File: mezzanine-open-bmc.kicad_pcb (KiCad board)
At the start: 2 copper layers, 85 x 54.1 mm, 48 parts, among them P1 CONN_02X20, P2 CONN_02X20, SW1 PWR, SW2 RST, U1 FT230XS, U2 PMIC-CJT1117-3.3(SOT223), U4 PCA9306

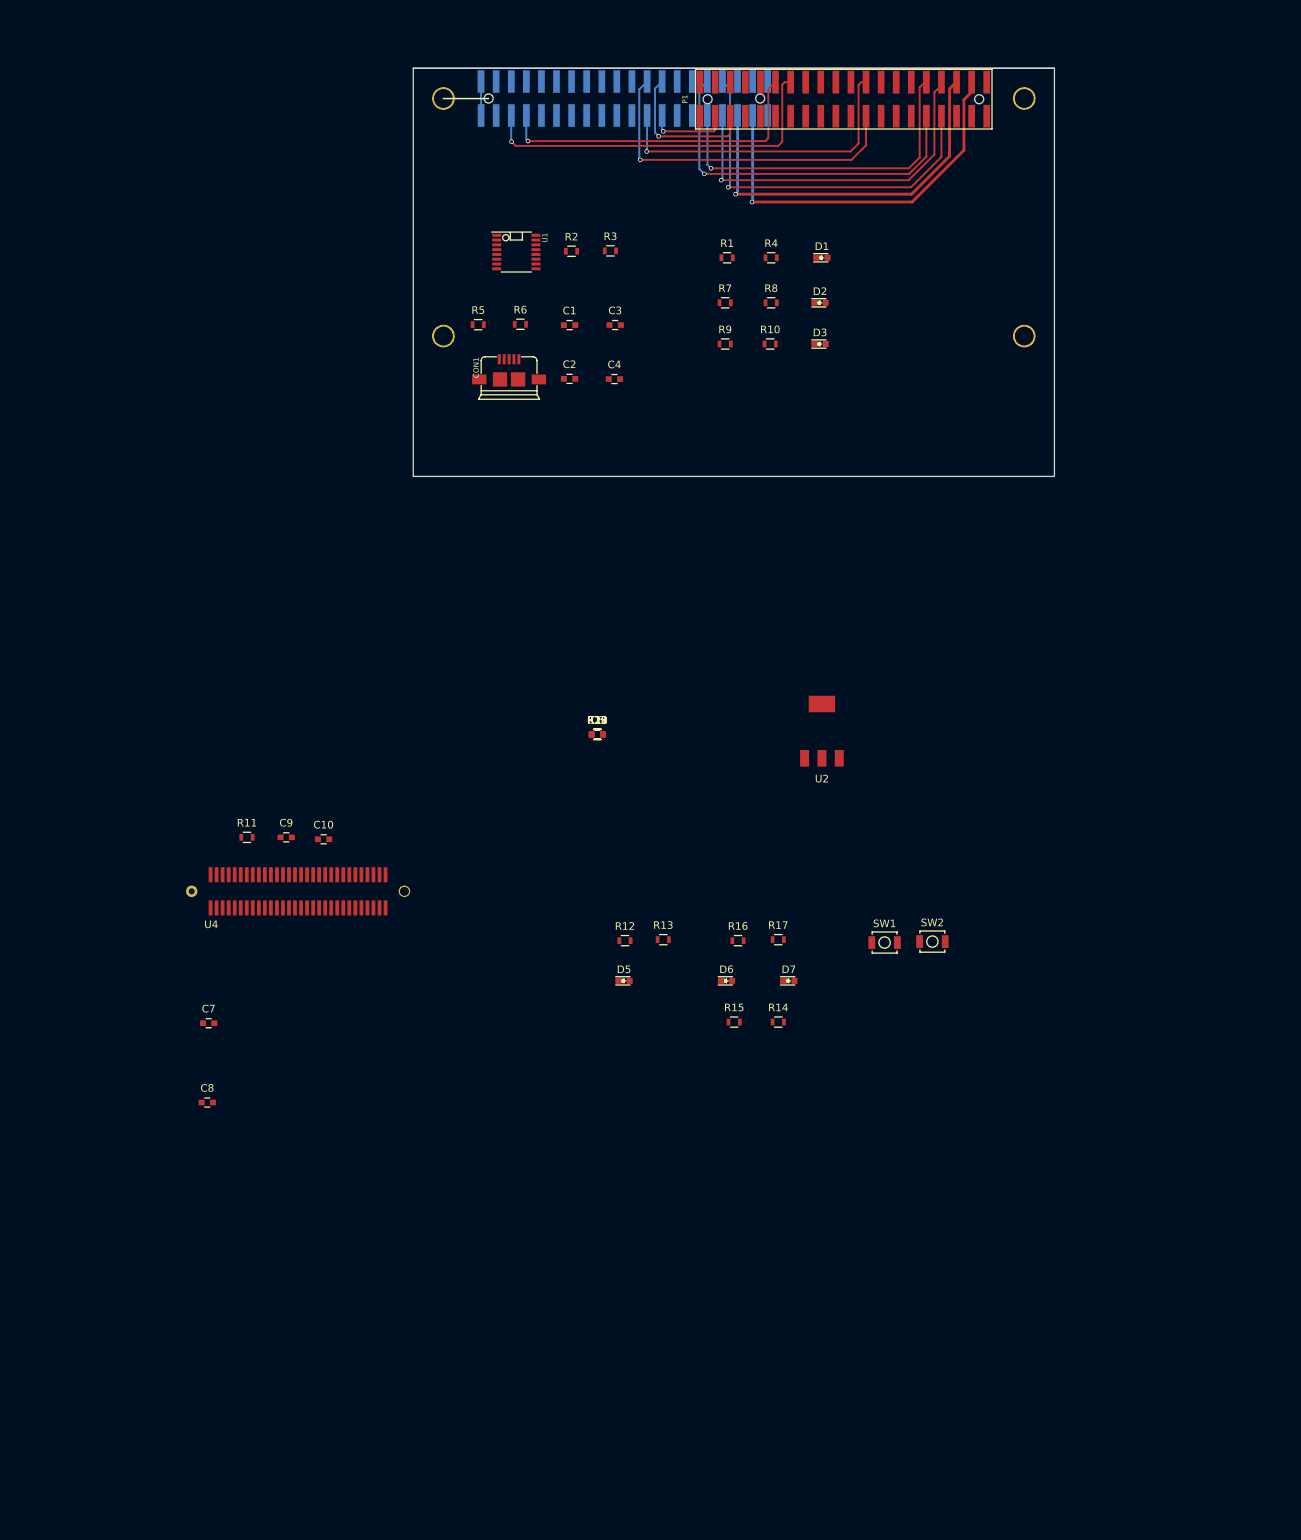
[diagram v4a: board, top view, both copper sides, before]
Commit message: Alternative Traces for Header Pins
Since most components will be sitting on the top side of the
device, traces for the header pins have been drawn on the bottom side
as much as possible. This should mean it will be easier to connect the
rest of the components.
A new branch has been made to preserve the former trace layout if this
version is no good.

Signed-off-by: Sophie Haynes <sophie.haynes@linaro.org>
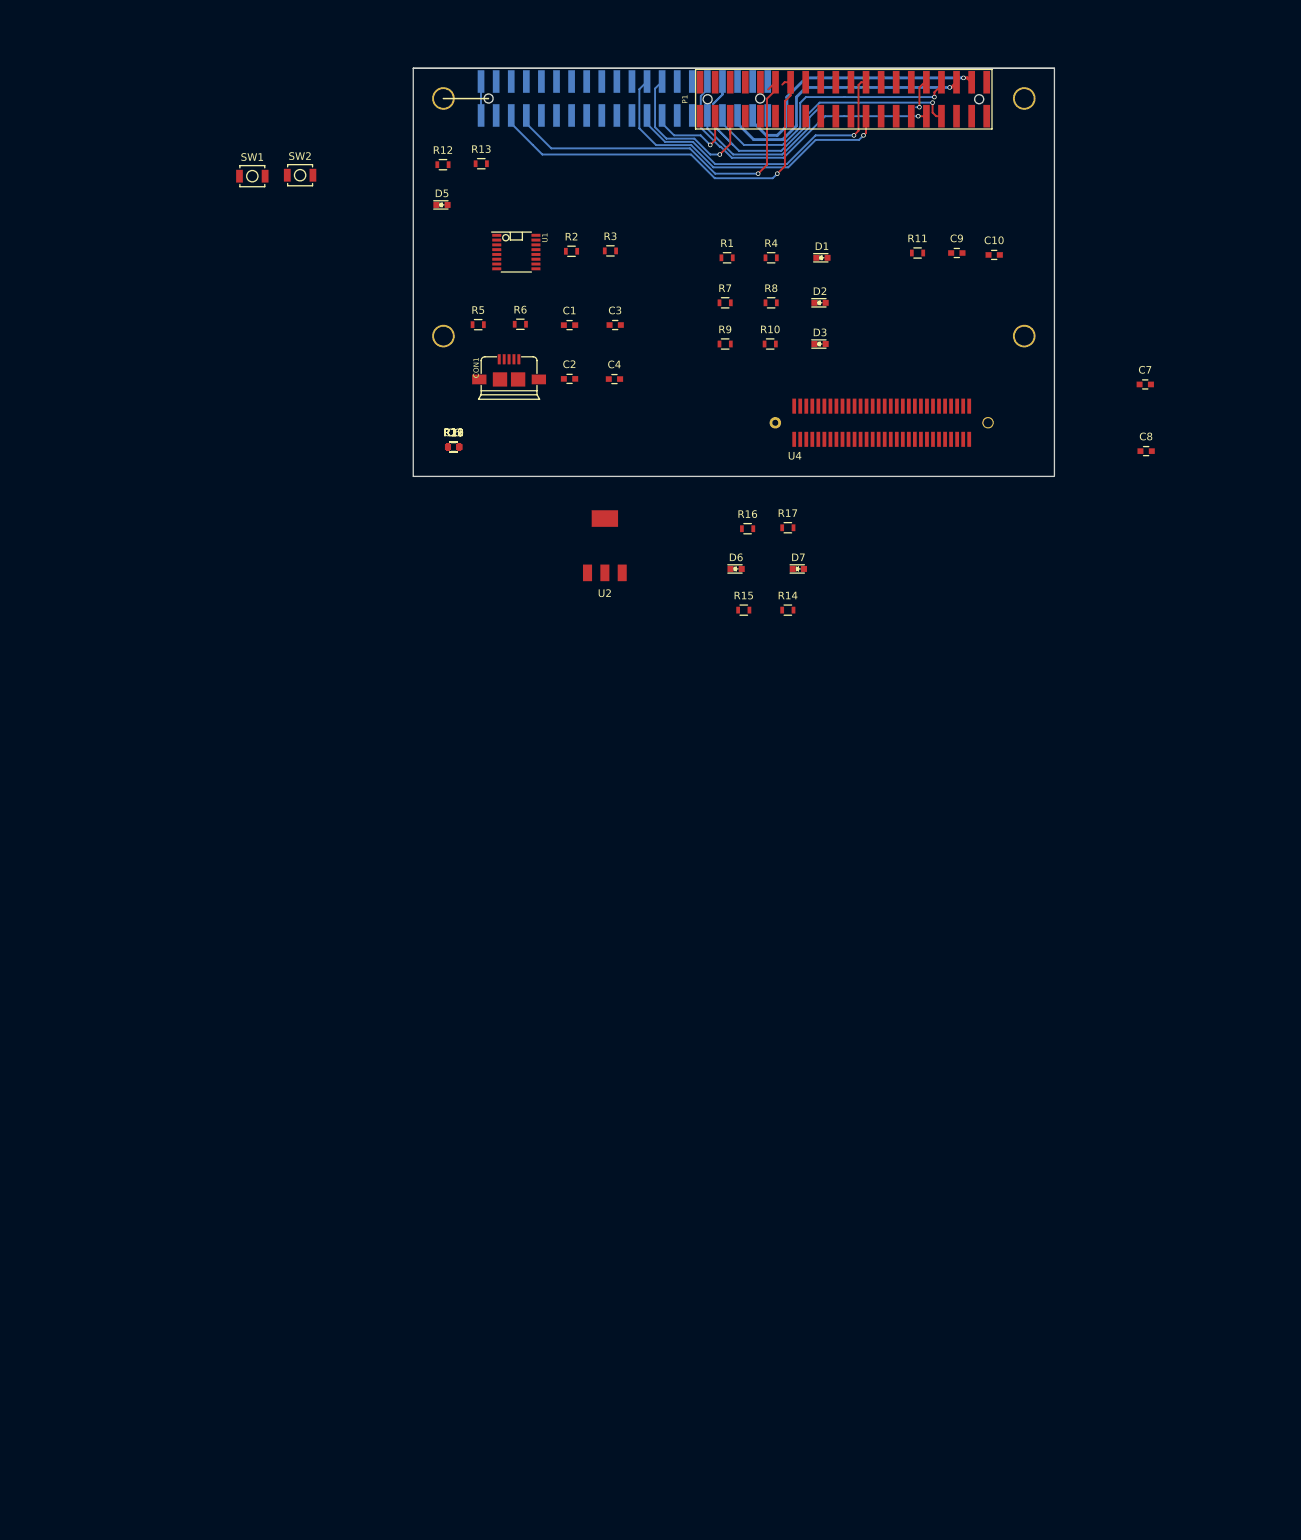
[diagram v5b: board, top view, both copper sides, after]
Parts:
- moved C8 151.5 mm to (197.2, 150.7)
- moved C7 150.3 mm to (197.0, 141.9)
- moved SW1 131.7 mm to (78.7, 114.3)
- moved SW2 131.7 mm to (85.0, 114.2)
- moved C10 117.9 mm to (177.0, 124.7)
- moved C9 117.9 mm to (172.1, 124.5)
- moved R11 117.9 mm to (166.9, 124.5)
- moved R13 105.7 mm to (109.0, 112.6)
- moved D5 105.7 mm to (103.8, 118.1)
- moved R12 105.7 mm to (103.9, 112.8)
- moved U4 99.2 mm to (150.5, 144.8)
- moved R14 54.6 mm to (149.7, 171.8)
- moved R15 54.6 mm to (143.8, 171.8)
- moved R17 54.6 mm to (149.7, 160.9)
- moved D6 54.6 mm to (142.8, 166.4)
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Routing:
- net GPIO_I: track 45.9 -> 25.7 mm
- net +1V8: track 51.2 -> 36.4 mm
- net +5V: track 51.9 -> 37.5 mm
- net GPIO_K: track 48.3 -> 37.2 mm
- net GPIO_J: track 48.7 -> 40.3 mm
- net UART0_RX_BMC: track 43.3 -> 49.0 mm
- net UART0_TX_BMC: track 48.7 -> 53.7 mm
- net GPIO_D_BMC: track 19.8 -> 24.5 mm
- net GPIO_L: track 49.9 -> 54.2 mm
- net GPIO_C_BMC: track 11.0 -> 14.5 mm
- net GPIO_B: track 45.4 -> 42.9 mm
- net GPIO_A: track 42.2 -> 40.4 mm

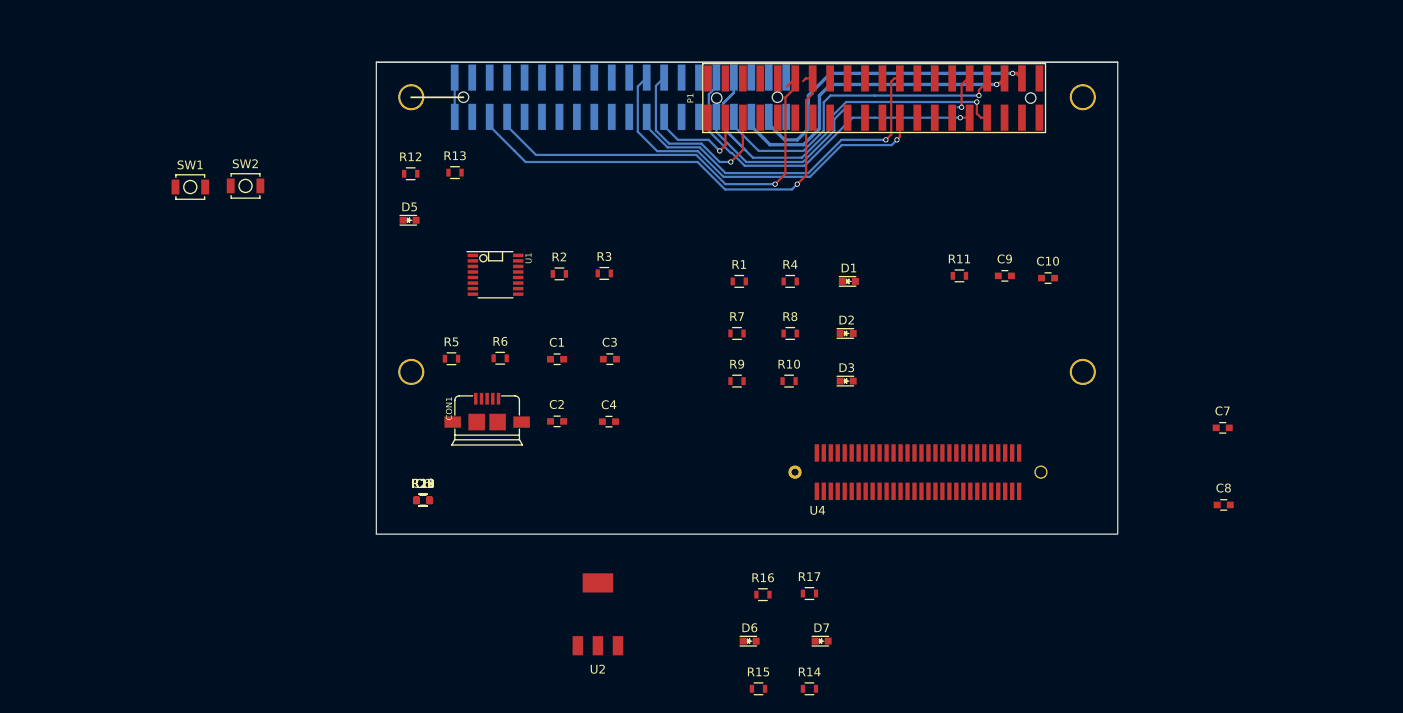
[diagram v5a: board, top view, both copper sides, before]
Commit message: Create Correct Footprint for PCA9306, Assign Footprint, Connect U4
The PCA footprint was incorrect. This has been fixed; there are two
different models so both types have been added. It has been assigned
accordingly in the schematic.

U4(level shifter 1.8-3.3v) has been connected up.

Signed-off-by: Sophie Haynes <sophie.haynes@linaro.org>
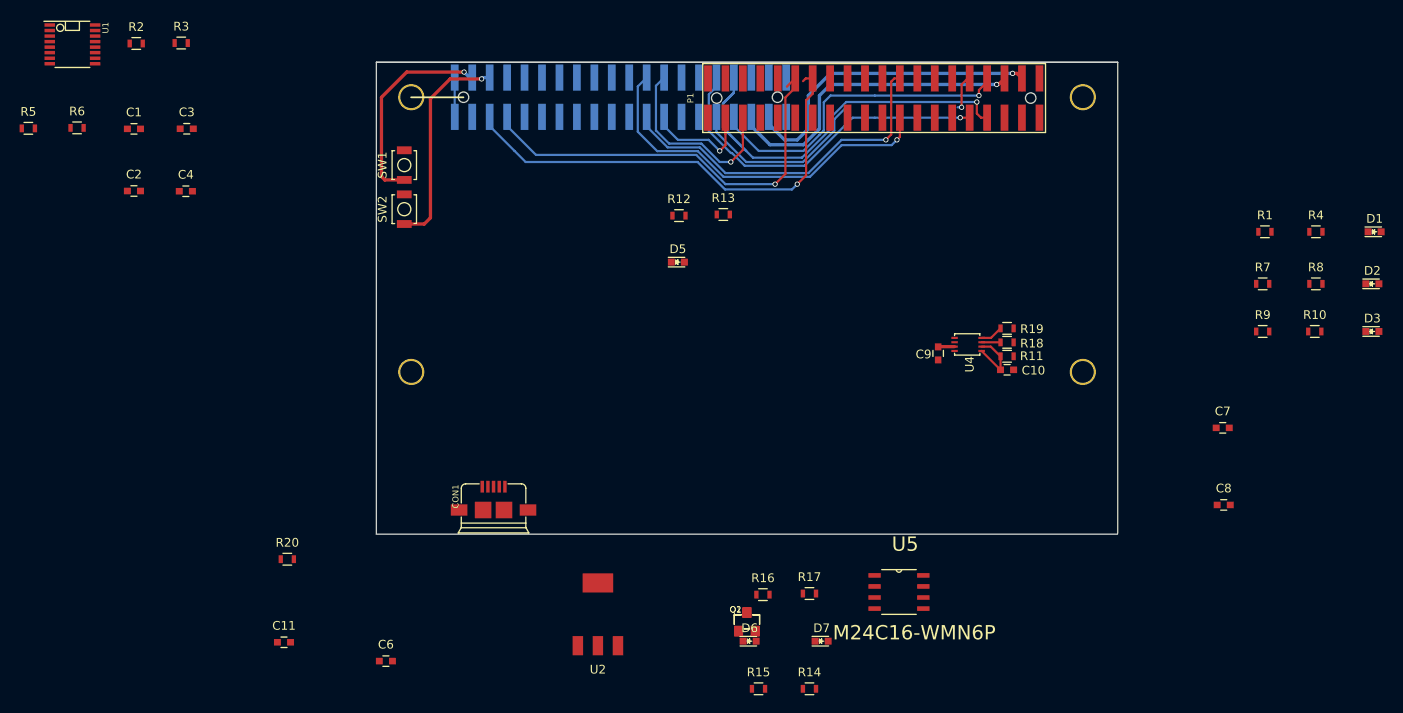
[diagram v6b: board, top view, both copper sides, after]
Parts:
- added Q1, Q2: S8050, 96boards:SOT-23_Seeed, F.Cu at (142.5, 164.2)
- added U5: M24C16-WMN6P, 96boards:SOIC127P600X175-8N, F.Cu at (159.9, 160.7)
- moved R19 69.8 mm to (172.3, 130.5), turned to 180 degrees
- moved R18 69.4 mm to (172.3, 132.1), turned to 180 degrees
- moved D1 60.5 mm to (214.5, 119.4)
- moved R1 60.5 mm to (201.9, 119.4)
- moved R10 60.5 mm to (207.6, 130.9)
- moved R7 60.5 mm to (201.6, 125.4)
- moved R9 60.5 mm to (201.6, 130.9)
- moved D2 60.5 mm to (214.2, 125.4)
- moved D3 60.5 mm to (214.2, 130.9)
- moved R4 60.5 mm to (207.7, 119.4)
- moved R8 60.5 mm to (207.7, 125.4)
- moved R2 55.2 mm to (72.5, 97.8)
- moved C3 55.2 mm to (78.3, 107.6)
- moved C2 55.2 mm to (72.2, 114.8)
- moved C4 55.2 mm to (78.2, 114.8)
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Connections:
- P2 pad 15: I2C0_SCL_BMC -> I2C0_SCL
- P2 pad 17: I2C0_SDA_BMC -> I2C0_SDA
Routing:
- net RST_BTN_BMC: track 0.00 -> 24.7 mm, vias 0 -> 1
- net PWR_BTN_BMC: track 0.00 -> 23.7 mm, vias 0 -> 1
- net Net-(C10-Pad1): track 0.00 -> 7.24 mm
- net Net-(R19-Pad2): track 0.00 -> 2.62 mm
- net Net-(R18-Pad2): track 0.00 -> 2.17 mm
- net +1V8: track 36.4 -> 38.3 mm

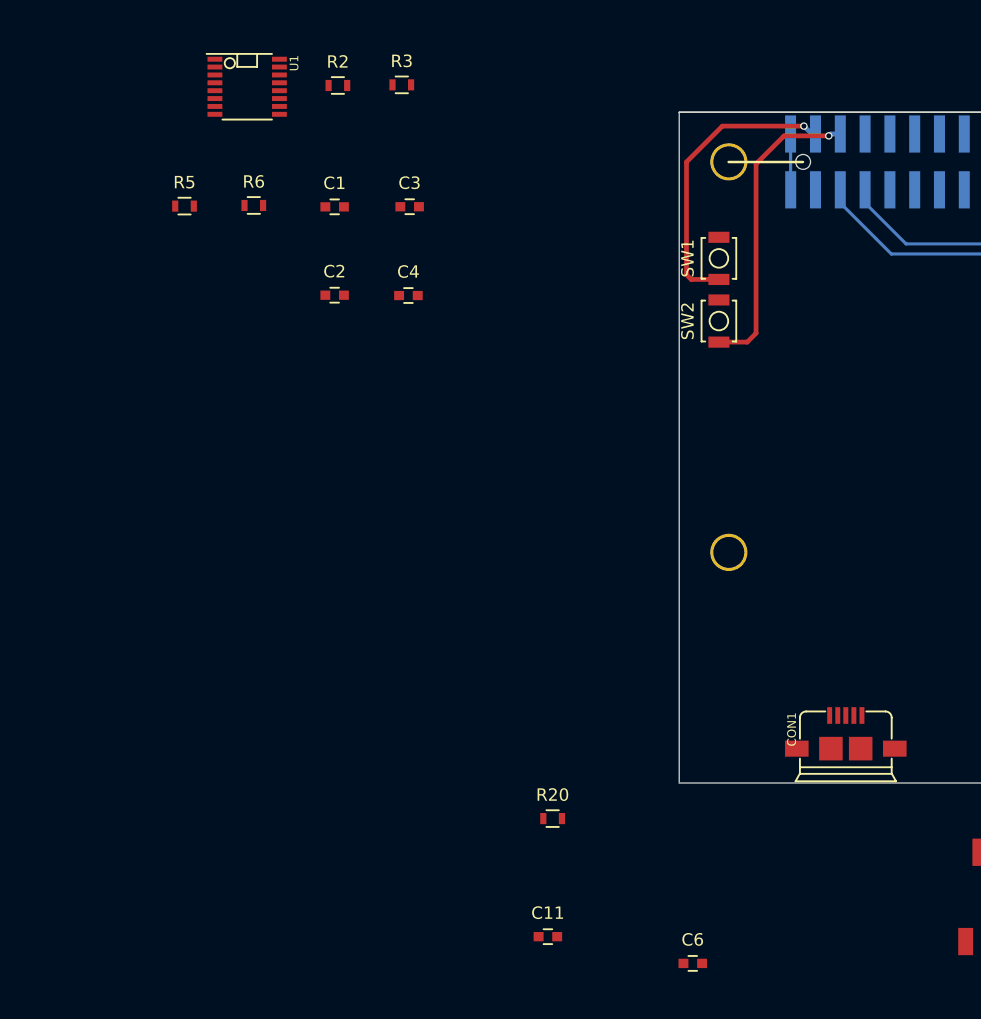
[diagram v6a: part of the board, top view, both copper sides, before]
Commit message: Wire Up FTDI
The wiring for the FTDI components have been connnected up in a neat
little bundle which can be placed on the board.

Signed-off-by: Sophie Haynes <sophie.haynes@linaro.org>
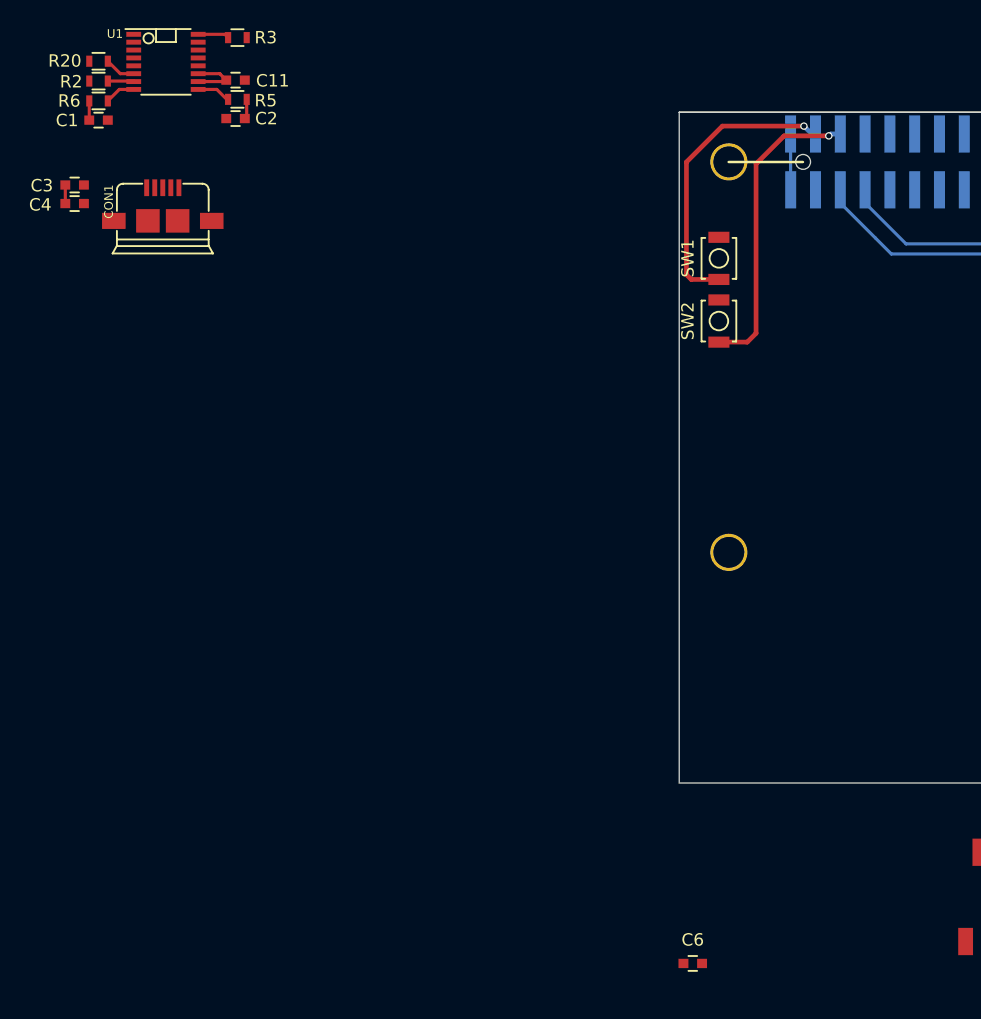
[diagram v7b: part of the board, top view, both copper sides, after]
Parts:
- moved C11 73.5 mm to (64.2, 97.4)
- moved R20 71.2 mm to (53.2, 95.9)
- moved CON1 69.6 mm to (58.3, 110.3)
- moved C4 27.9 mm to (51.2, 107.4)
- moved C3 27.1 mm to (51.2, 105.9)
- moved C1 20.3 mm to (53.2, 100.6)
- moved R2 19.3 mm to (53.2, 97.5)
- moved C2 16.3 mm to (64.2, 100.5), turned to 180 degrees
- moved R6 15.1 mm to (53.2, 99.1), turned to 180 degrees
- moved R3 13.8 mm to (64.4, 94.0), turned to 180 degrees
- moved R5 9.61 mm to (64.4, 99.0)
- moved U1 6.85 mm to (58.6, 95.9)
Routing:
- net Net-(C11-Pad1): track 0.00 -> 4.79 mm
- net Net-(R5-Pad1): track 0.00 -> 2.75 mm
- net Net-(R3-Pad2): track 0.00 -> 2.53 mm
- net Net-(R20-Pad2): track 0.00 -> 2.50 mm
- net Net-(R6-Pad1): track 0.00 -> 2.47 mm
- net Net-(R2-Pad2): track 0.00 -> 2.10 mm
- net Net-(C2-Pad1): track 0.00 -> 1.61 mm
- net Net-(C1-Pad1): track 0.00 -> 1.55 mm
- net VBUS: track 0.00 -> 1.50 mm
